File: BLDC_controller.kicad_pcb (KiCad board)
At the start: 2 copper layers, 71 parts, among them Q1 PSMN2R0-30YLD, Q2 PSMN2R0-30YLD, Q3 PSMN2R0-30YLD, Q4 PSMN2R0-30YLD, Q5 PSMN2R0-30YLD, Q6 PSMN2R0-30YLD

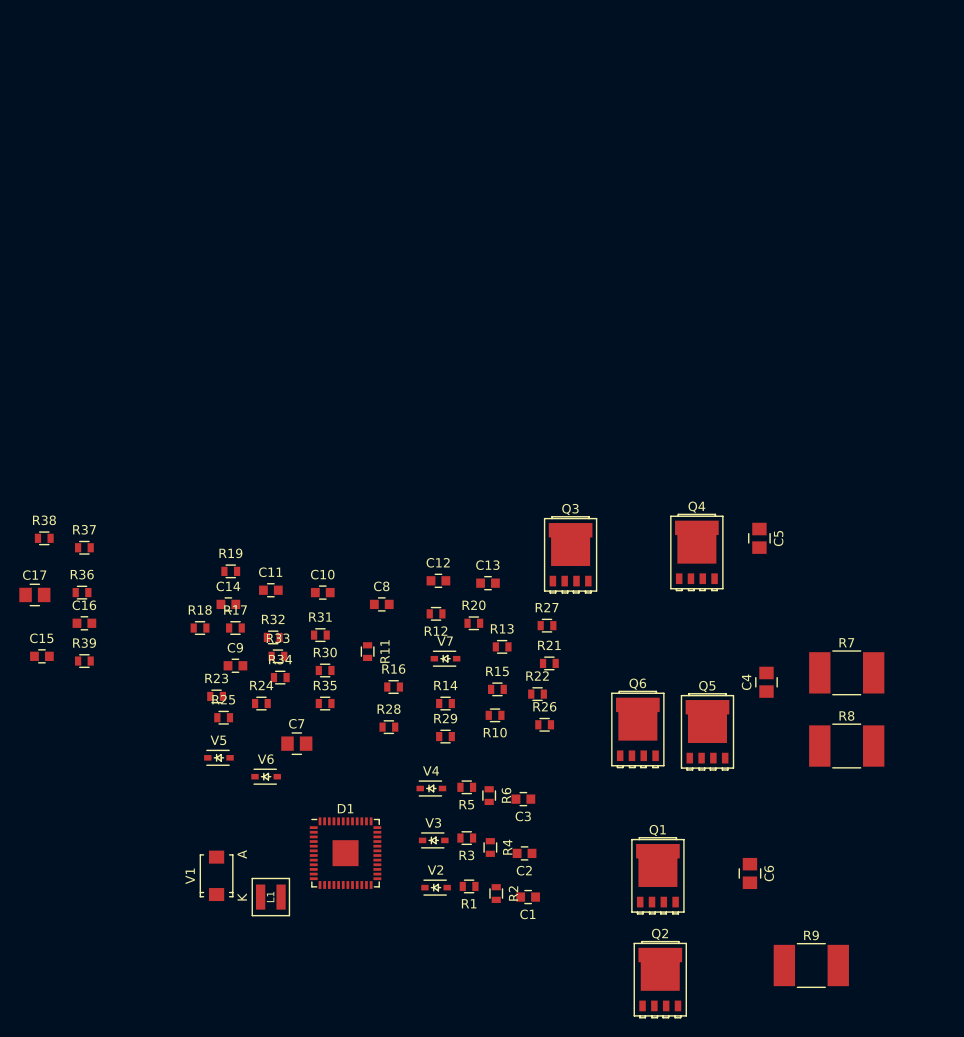
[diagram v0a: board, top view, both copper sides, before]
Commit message: most footprints selected
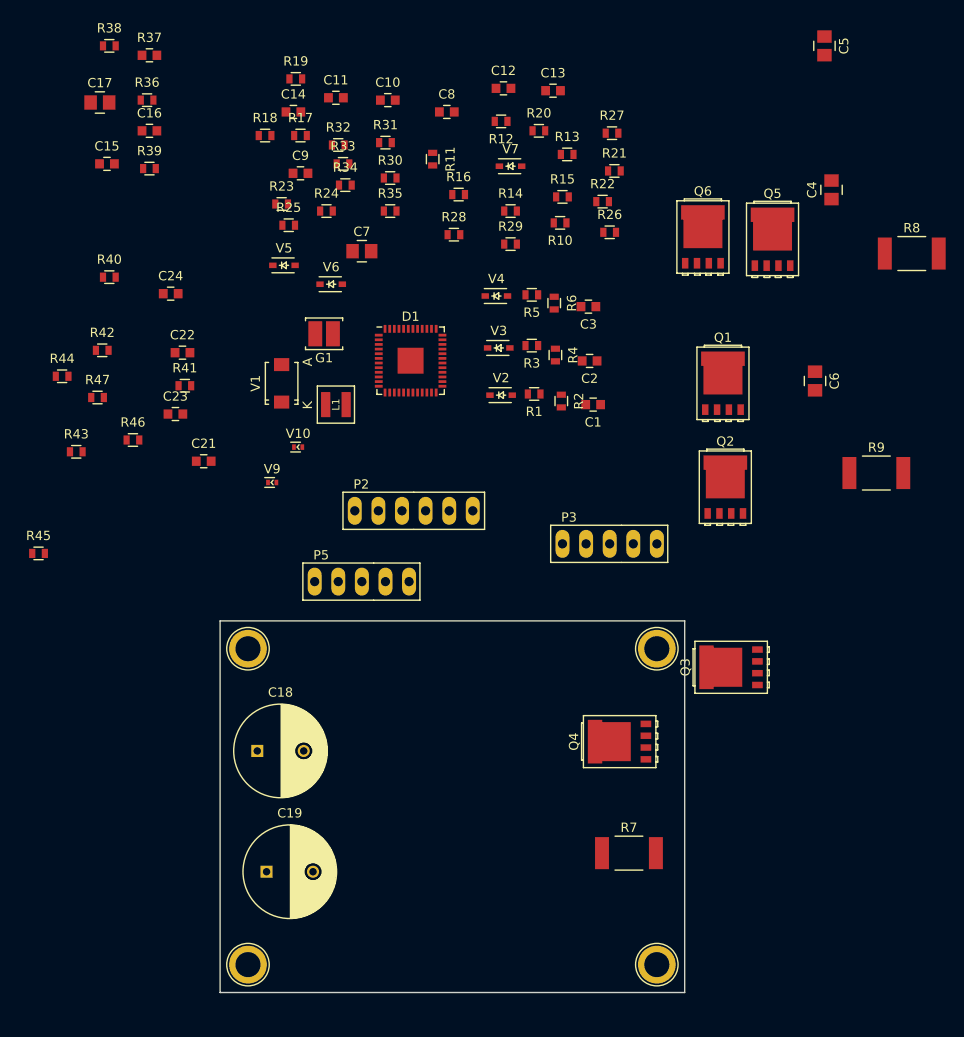
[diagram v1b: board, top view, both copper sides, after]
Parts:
- added C18: 220u, project_footprints:C_Radial_D10_L25_P5, F.Cu at (139.0, 94.0)
- added C19: 220u, project_footprints:C_Radial_D10_L25_P5, F.Cu at (140.0, 107.0)
- added C21: C, project_footprints:C_0603, F.Cu at (133.2, 62.8)
- added C22: 10p, project_footprints:C_0603, F.Cu at (131.0, 51.1)
- added C23: 10p, project_footprints:C_0603, F.Cu at (130.2, 57.7)
- added C24: 10p, project_footprints:C_0603, F.Cu at (129.7, 44.8)
- added G1: NX3225GD, project_footprints:Crystal_3225, F.Cu at (146.2, 49.1)
- added P2: CONN_01X06, project_footprints:PINHEAD1-6, F.Cu at (155.8, 68.2)
- added P3: CONN_01X05, project_footprints:PINHEAD1-5, F.Cu at (176.9, 71.7)
- added P5: CONN_01X05, project_footprints:PINHEAD1-5, F.Cu at (150.3, 75.8)
- added R40: 2k2, project_footprints:R_0603, F.Cu at (123.1, 43.0)
- added R41: 1k0, project_footprints:R_0603, F.Cu at (131.2, 54.7)
- added R42: 1k0, project_footprints:R_0603, F.Cu at (122.3, 50.9)
- added R43: 1k0, project_footprints:R_0603, F.Cu at (119.5, 61.8)
- added R44: 10k, project_footprints:R_0603, F.Cu at (118.0, 53.7)
- added R45: 10k, project_footprints:R_0603, F.Cu at (115.5, 72.7)
- added R46: 10k, project_footprints:R_0603, F.Cu at (125.6, 60.5)
- added R47: 10R, project_footprints:R_0603, F.Cu at (121.8, 56.0)
- added REF**: 1pin, Connect:1pin, F.Cu at (138.0, 83.0)
- added REF**: 1pin, Connect:1pin, F.Cu at (182.0, 117.0)
- added REF**: 1pin, Connect:1pin, F.Cu at (138.0, 117.0)
- added REF**: 1pin, Connect:1pin, F.Cu at (182.0, 83.0)
- added V10: LED_ALT, project_footprints:LED_0402, F.Cu at (143.4, 61.3)
- added V9: LED_ALT, project_footprints:LED_0402, F.Cu at (140.6, 65.1)
- C15: value 4n7 -> C
- R10: value 75k -> 46k4
- R36: value 169k -> 2k2
- R37: value 9k31 -> 10R; footprint project_footprints:R_0603 -> project_footprints:C_0603
- R7, R8, R9: footprint project_footprints:R_2816 -> project_footprints:R_2512
- moved C4 53.5 mm to (200.8, 33.6)
- moved D1 53.5 mm to (155.5, 52.0)
- moved R14 53.5 mm to (166.3, 35.9)
- moved R15 53.5 mm to (171.8, 34.4)
- moved R17 53.5 mm to (143.7, 27.8)
- moved R18 53.5 mm to (139.8, 27.8)
- moved R23 53.5 mm to (141.6, 35.1)
- moved R24 53.5 mm to (146.4, 35.9)
- moved R25 53.5 mm to (142.4, 37.4)
- moved R26 53.5 mm to (176.9, 38.2)
- moved R31 53.5 mm to (152.8, 28.5)
- moved R35 53.5 mm to (153.3, 35.9)
- moved R4 53.5 mm to (171.1, 51.4)
- moved V3 53.5 mm to (165.0, 50.6)
- moved V5 53.5 mm to (141.9, 41.7)
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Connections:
- net Net-(C16-Pad1) renamed /NRST
- net Net-(C8-Pad1) renamed /OC_COMP
- net Net-(D1-Pad9) renamed /SW
- C1 pad 1: /OUTW -> /OUTU
- C10 pad 1: PA4 -> /V_ADC
- C11 pad 1: PA5 -> /U_ADC
- C12 pad 1: Net-(C12-Pad1) -> +12V
- C15 pad 1: Net-(C15-Pad1) -> /OSC_IN
- C17 pad 1: Net-(C17-Pad1) -> +12V
- C3 pad 1: /OUTU -> /OUTW
- C9 pad 1: PA3 -> /W_ADC
- D1 pad 11: Net-(D1-Pad11) -> /U_ADC
- D1 pad 12: Net-(D1-Pad12) -> /V_ADC
- D1 pad 14: PA3 -> /HALL1/A+
- D1 pad 15: PA4 -> /SPI1_NSS
- D1 pad 16: PA5 -> /SPI1_SCK
- D1 pad 17: Net-(D1-Pad17) -> /SPI1_MISO
- D1 pad 18: Net-(D1-Pad18) -> /SPI1_MOSI
- D1 pad 19: Net-(C15-Pad1) -> /W_ADC
- D1 pad 20: Net-(D1-Pad20) -> GND
- D1 pad 21: PA3 -> /W_ADC
- D1 pad 27: Net-(C1-Pad2) -> Net-(C3-Pad2)
- D1 pad 3: Net-(D1-Pad2) -> Net-(D1-Pad3)
- D1 pad 35: Net-(C3-Pad2) -> Net-(C1-Pad2)
- D1 pad 37: Net-(D1-Pad37) -> /SWDIO
- D1 pad 38: Net-(D1-Pad38) -> /SWCLK
- D1 pad 39: /UART1_TX -> /HALL2/B+
- D1 pad 4: Net-(D1-Pad4) -> /OSC_IN
- D1 pad 40: /UART1_RX -> /HALL3/Z+
- D1 pad 43: PA4 -> /V_ADC
- D1 pad 47: PA5 -> /U_ADC
- D1 pad 6: Net-(C12-Pad1) -> +12V
- D1 pad 8: Net-(C17-Pad1) -> +12V
- Q1 pad 1: /OUTW -> /OUTU
- Q1 pad 2: /OUTW -> /OUTU
- Q1 pad 3: /OUTW -> /OUTU
- Q1 pad 4: /HSW -> /HSU
- Q2 pad 1: W_SENSE_P -> U_SENSE_P
- Q2 pad 2: W_SENSE_P -> U_SENSE_P
- Q2 pad 3: W_SENSE_P -> U_SENSE_P
- Q2 pad 4: /LSW -> /LSU
- Q2 pad 5: /OUTW -> /OUTU
- Q3 pad 1: /OUTU -> /OUTW
- Q3 pad 2: /OUTU -> /OUTW
- Q3 pad 3: /OUTU -> /OUTW
- Q3 pad 4: /HSU -> /HSW
- Q4 pad 1: U_SENSE_P -> W_SENSE_P
- Q4 pad 2: U_SENSE_P -> W_SENSE_P
- Q4 pad 3: U_SENSE_P -> W_SENSE_P
- Q4 pad 4: /LSU -> /LSW
- Q4 pad 5: /OUTU -> /OUTW
- R1 pad 1: /HSW -> /HSU
- R14 pad 1: U_SENSE_N -> W_SENSE_N
- R15 pad 1: W_SENSE_N -> U_SENSE_N
- R2 pad 1: /HSW -> /HSU
- R2 pad 2: Net-(D1-Pad25) -> Net-(D1-Pad33)
- R26 pad 1: PA3 -> /W_ADC
- R27 pad 1: PA4 -> /V_ADC
- R28 pad 1: PA5 -> /U_ADC
- R30 pad 1: /LSW -> /LSU
- R31 pad 1: /LSW -> /LSU
- R31 pad 2: Net-(D1-Pad28) -> Net-(D1-Pad36)
- R34 pad 1: /LSU -> /LSW
- R35 pad 1: /LSU -> /LSW
- R35 pad 2: Net-(D1-Pad36) -> Net-(D1-Pad28)
- R36 pad 1: Net-(C17-Pad1) -> +3V3
- R36 pad 2: Net-(C15-Pad1) -> /SPI1_NSS
- R37 pad 1: Net-(C15-Pad1) -> Net-(D1-Pad5)
- R37 pad 2: GND -> Net-(C21-Pad1)
- R5 pad 1: /HSU -> /HSW
- R6 pad 1: /HSU -> /HSW
- R6 pad 2: Net-(D1-Pad33) -> Net-(D1-Pad25)
- R7 pad 1: U_SENSE_P -> W_SENSE_P
- R9 pad 1: W_SENSE_P -> U_SENSE_P
- V2 pad 1: Net-(D1-Pad25) -> Net-(D1-Pad33)
- V4 pad 1: Net-(D1-Pad33) -> Net-(D1-Pad25)
- V5 pad 1: Net-(D1-Pad28) -> Net-(D1-Pad36)
- V7 pad 1: Net-(D1-Pad36) -> Net-(D1-Pad28)
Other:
- board outline added: 50 x 40 mm

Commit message: parts in place
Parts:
- added C20: 220n, project_footprints:C_0805, B.Cu at (174.5, 83.0)
- added C25: 220n, project_footprints:C_0805, F.Cu at (178.0, 92.0)
- added C26: 220n, project_footprints:C_0805, F.Cu at (182.5, 100.8)
- added C27: 220n, project_footprints:C_0805, B.Cu at (173.8, 110.5)
- C10, C11, C22, C23, C24, C9: footprint project_footprints:C_0603 -> project_footprints:C_0402; moved to B.Cu
- C15, C16, C21, C8: footprint project_footprints:C_0603 -> project_footprints:C_0402
- C18: value 220u -> 680u
- C19: value 220u -> 220n; footprint project_footprints:C_Radial_D10_L25_P5 -> project_footprints:C_0805
- Q2, Q4, Q6, R7, R8, R9, V5, V6, V7: moved to B.Cu
- R1, R2, R3, R4, R40, R5, R6: footprint project_footprints:R_0603 -> project_footprints:R_0603_NOM
- R10, R36, R38, R39: footprint project_footprints:R_0603 -> project_footprints:R_0402_MOST
- R11, R12, R13, R14, R15, R16, R17, R18, R19, R20, R21, R22, R23, R24, R25, R26, R27, R28, R29, R41, R42, R43, R44, R45, R46, R47: footprint project_footprints:R_0603 -> project_footprints:R_0402_MOST; moved to B.Cu
- R30, R31, R32, R33, R34, R35: footprint project_footprints:R_0603 -> project_footprints:R_0603_NOM; moved to B.Cu
- R37: footprint project_footprints:C_0603 -> project_footprints:R_0402_MOST
- moved R36 84.0 mm to (156.6, 102.6)
- moved R38 83.4 mm to (141.4, 99.5), turned to 180 degrees
- moved C16 82.5 mm to (153.5, 105.5), turned to 270 degrees
- moved R17 81.0 mm to (164.5, 106.0)
- moved R20 80.1 mm to (157.8, 106.5), turned to 270 degrees
- moved C9 78.7 mm to (161.5, 108.5)
- moved C5 78.5 mm to (173.5, 92.0), turned to 180 degrees
- moved C17 77.7 mm to (153.8, 95.1), turned to 90 degrees
- moved R37 77.6 mm to (130.4, 96.7), turned to 90 degrees
- moved C8 77.4 mm to (163.0, 102.5)
- moved R39 77.0 mm to (154.0, 103.6), turned to 180 degrees
- moved C14 74.9 mm to (154.4, 99.3), turned to 90 degrees
- moved R11 74.8 mm to (161.8, 105.0), turned to 180 degrees
- moved R23 74.1 mm to (156.2, 107.8), turned to 270 degrees
- moved C10 73.6 mm to (162.0, 97.0)
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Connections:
- D1 pad 13: Net-(D1-Pad13) -> (no net)
- P2 pad 6: Net-(P2-Pad6) -> (no net)
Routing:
- net /LSU: track 0.00 -> 12.0 mm
- net /HSV: track 0.00 -> 10.8 mm
- net /LSV: track 0.00 -> 10.7 mm
- net GND: track 0.00 -> 4.20 mm, vias 0 -> 1
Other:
- board size 50 x 40 mm -> 50 x 35 mm
- net class Default: via_dia 0.6 -> 0.8
- net class Medium_Power added: clearance 0.2, trace_width 0.5, via_dia 0.8, via_drill 0.4

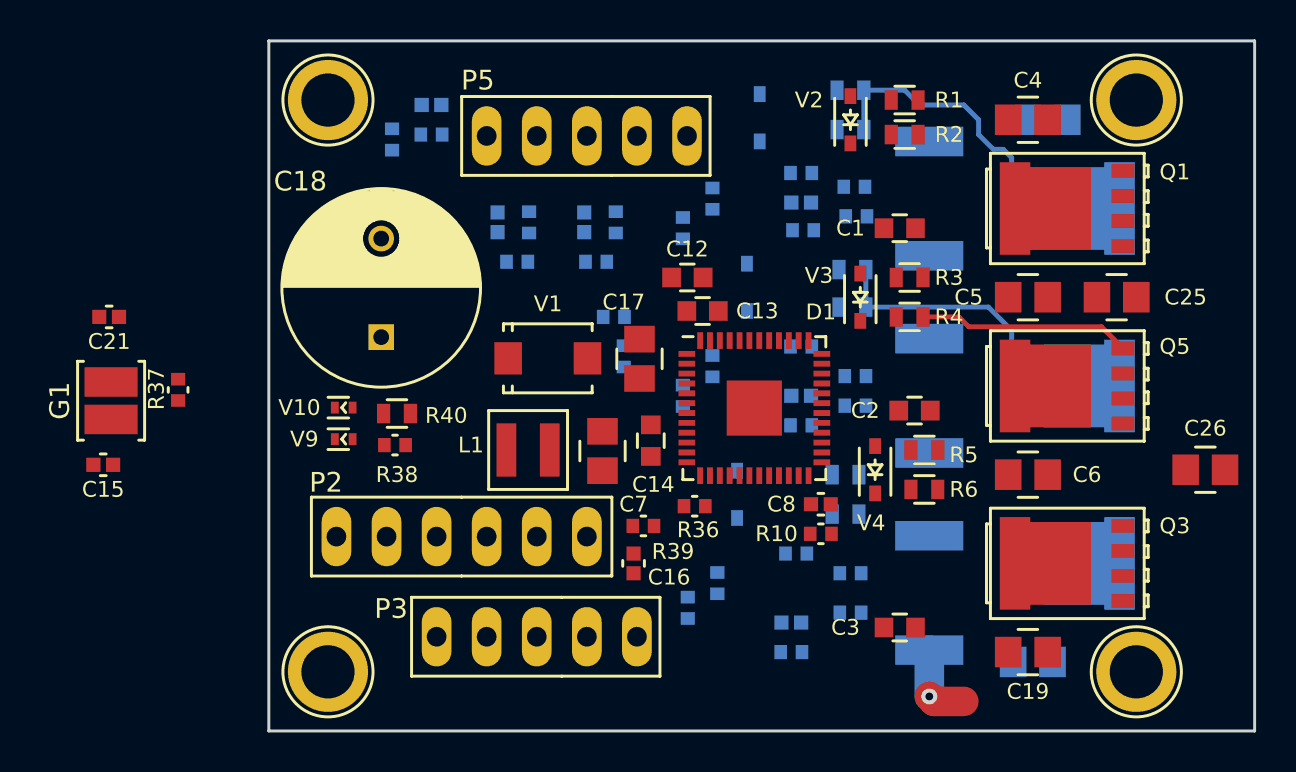
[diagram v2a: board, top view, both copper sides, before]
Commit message: mostly routed
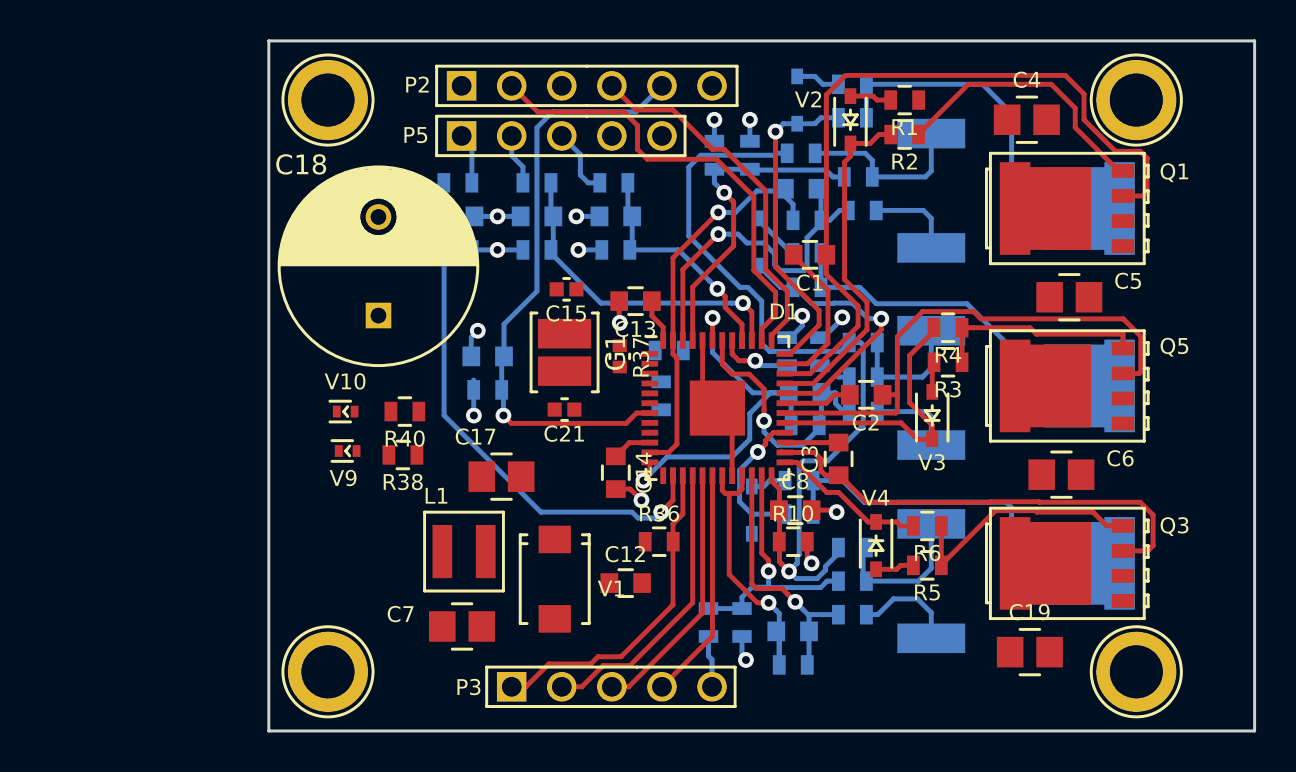
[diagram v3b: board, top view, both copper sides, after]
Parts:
- removed C20, C25, C26, C27: 220n, project_footprints:C_0805
- C10, C11, C22, C23, C24, C8, C9: footprint project_footprints:C_0402 -> project_footprints:C_0603
- C16: footprint project_footprints:C_0402 -> project_footprints:C_0603; moved to B.Cu
- R1, R2, R3, R30, R31, R32, R33, R34, R35, R4, R40, R5, R6: footprint project_footprints:R_0603_NOM -> project_footprints:R_0603
- R10, R11, R12, R13, R14, R15, R16, R17, R18, R19, R20, R21, R22, R23, R24, R25, R26, R27, R28, R29, R36, R38, R41, R42, R43, R44, R45, R46, R47: footprint project_footprints:R_0402_MOST -> project_footprints:R_0603
- R39: footprint project_footprints:R_0402_MOST -> project_footprints:R_0603; moved to B.Cu
- moved C15 25.1 mm to (150.1, 91.6)
- moved P2 23.7 mm to (151.1, 81.3), turned to 0 degrees
- moved C21 23.6 mm to (150.0, 97.7)
- moved G1 23.1 mm to (150.0, 94.8), turned to 270 degrees
- moved R37 22.5 mm to (152.8, 95.0), turned to 270 degrees
- moved C12 15.8 mm to (153.1, 106.5)
- moved C16 12.8 mm to (146.1, 95.0), turned to 180 degrees
- moved C7 11.4 mm to (144.8, 108.7), turned to 0 degrees
- moved V1 11.2 mm to (149.5, 106.3), turned to 270 degrees
- moved R39 10.5 mm to (146.1, 96.7), turned to 0 degrees
- moved C17 9.20 mm to (146.8, 101.1), turned to 180 degrees
- moved C3 9.09 mm to (163.9, 100.2), turned to 90 degrees
- moved V3 7.02 mm to (168.7, 98.0)
- moved R44 6.53 mm to (144.6, 89.6), turned to 180 degrees
- moved L1 6.09 mm to (144.9, 104.9), turned to 90 degrees
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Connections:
- net Net-(C1-Pad2) renamed /VBOOSTU
- net Net-(C2-Pad2) renamed /VBOOSTV
- net Net-(C3-Pad2) renamed /VBOOSTW
- net Net-(D1-Pad1) renamed /OP4P
- net Net-(D1-Pad2) renamed /OP4N
- net Net-(D1-Pad23) renamed /OP1P
- net Net-(D1-Pad41) renamed /OP2P
- net Net-(D1-Pad45) renamed /OP3P
- C10 pad 2: V_SENSE_N -> /OP2N
- C11 pad 2: U_SENSE_N -> /OP3N
- C9 pad 2: W_SENSE_N -> /OP1N
- D1 pad 22: W_SENSE_N -> /OP1N
- D1 pad 42: V_SENSE_N -> /OP2N
- D1 pad 46: U_SENSE_N -> /OP3N
- R14 pad 1: W_SENSE_N -> GND
- R14 pad 2: GND -> /OP1N
- R15 pad 1: U_SENSE_N -> GND
- R15 pad 2: GND -> /OP3N
- R16 pad 1: V_SENSE_N -> GND
- R16 pad 2: GND -> /OP2N
- R26 pad 2: W_SENSE_N -> /OP1N
- R27 pad 2: V_SENSE_N -> /OP2N
- R28 pad 2: U_SENSE_N -> /OP3N
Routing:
- net /OC_COMP: track 0.00 -> 44.1 mm, vias 0 -> 1
- net /OUTU: track 0.00 -> 39.4 mm
- net /NRST: track 0.00 -> 30.4 mm, vias 0 -> 1
- net GND: track 4.20 -> 33.6 mm, vias 1 -> 8
- net /HALL1/A+: track 0.00 -> 27.5 mm, vias 0 -> 1
- net /OUTV: track 0.00 -> 26.6 mm
- net /OUTW: track 0.00 -> 23.7 mm
- net /SWCLK: track 0.00 -> 23.4 mm
- net /V_ADC: track 0.00 -> 20.7 mm, vias 0 -> 2
- net /U_ADC: track 0.00 -> 20.2 mm, vias 0 -> 1
- net /SWDIO: track 0.00 -> 18.4 mm
- net /OP3N: track 0.00 -> 17.8 mm, vias 0 -> 1
- net Net-(D1-Pad33): track 0.00 -> 17.7 mm
- net /OP3P: track 0.00 -> 16.7 mm, vias 0 -> 1
- net /SPI1_NSS: track 0.00 -> 16.7 mm
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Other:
- copper layers 2 -> 4
